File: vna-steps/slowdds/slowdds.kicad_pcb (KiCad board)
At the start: 2 copper layers, 28 x 25.5 mm, 35 parts, among them P1 PWRCONN, P2 SWD_CONN, P3 UART_CONN, P4 DDSOUT_SMA, U1 25MHz, U2 FAN2558S33X, U3 FAN2558S33X, U4 STM32F030F4, U5 AD9833, U6 ADA4853-1

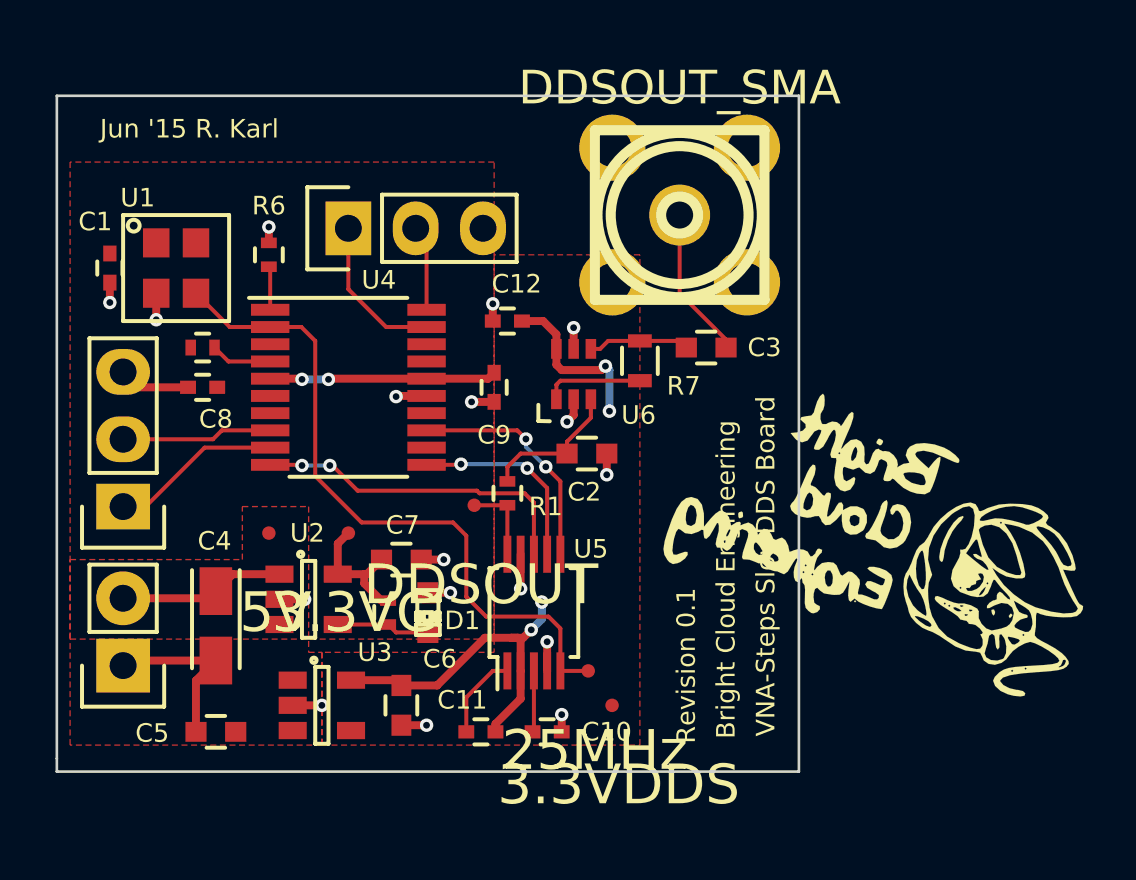
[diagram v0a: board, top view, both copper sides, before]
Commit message: Add design document specification for USB power stick.
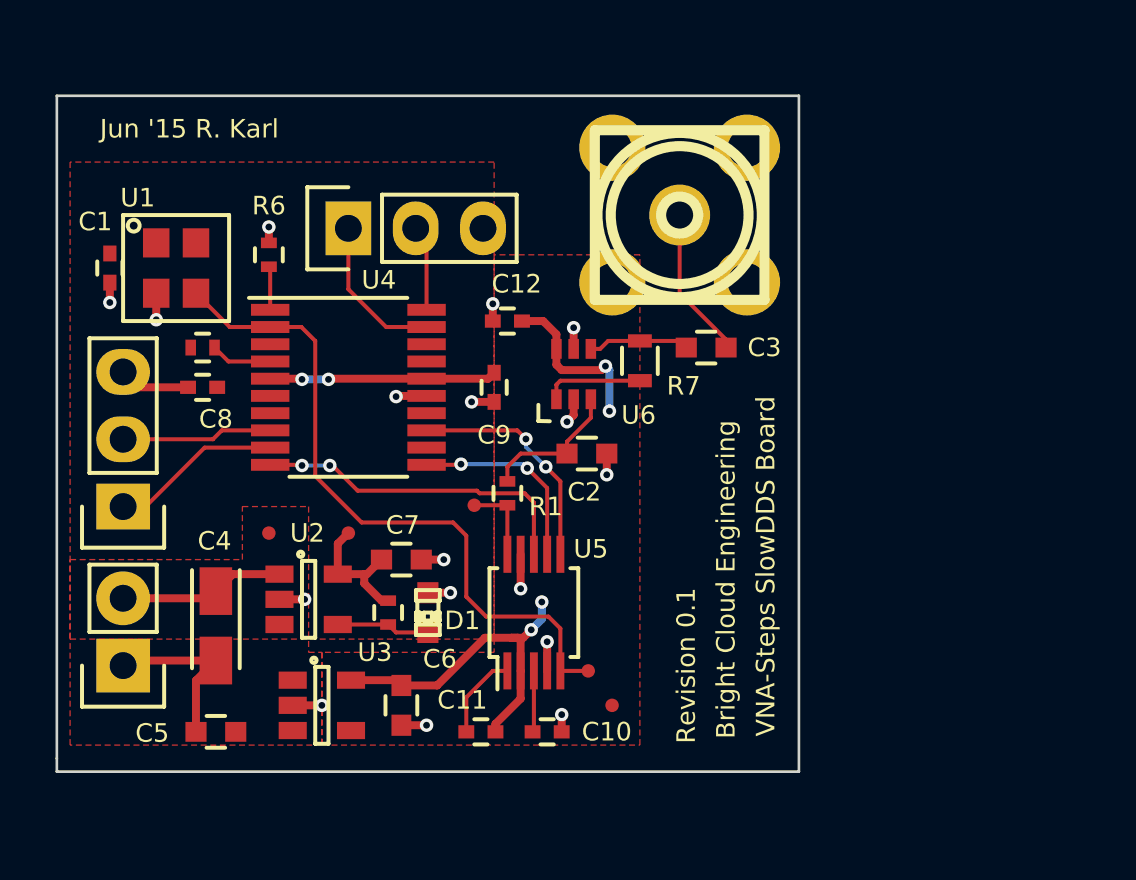
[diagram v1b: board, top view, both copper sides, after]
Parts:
- removed the G*** at (148.5, 78.0)
